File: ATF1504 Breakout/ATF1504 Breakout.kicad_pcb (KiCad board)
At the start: 2 copper layers, 73 x 52.5 mm, 12 parts, among them J1 Conn_01x20_Pin, J2 Conn_01x20_Pin, J3 Conn_01x02_Pin, P1 HDR-IDC-2.54-2X5P, U1 ATF1504ASV-xAx44, U2 TLV1117LV33DCYR

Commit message: route tracks and add graphics
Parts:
- added C3: 0.01u, easyeda2kicad:C0603, F.Cu at (175.8, 104.1)
- added R1: CLK ~{E}, easyeda2kicad:R0805, F.Cu at (176.0, 117.9)
- added REF**: KiCad-Logo_5mm_SilkScreen, Symbol:KiCad-Logo_5mm_SilkScreen, B.Cu at (180.9, 97.8)
- added REF**: OSHW-Logo2_9.8x8mm_SilkScreen, Symbol:OSHW-Logo2_9.8x8mm_SilkScreen, B.Cu at (180.1, 122.2)
- added U3: DSC1001CI4-002.0480T, easyeda2kicad:OSC-SMD_4P-L3.2-W2.5-BL_1C210000BB0F, F.Cu at (176.0, 110.3)
- C1, C2: value C_Polarized -> 1u; footprint easyeda2kicad:CAP-SMD_BD4.0-L4.3-W4.3-FD -> easyeda2kicad:C0603
- moved C2 16.3 mm to (190.3, 110.0)
- moved C1 11.5 mm to (185.5, 110.0), turned to 180 degrees
- moved U2 2.46 mm to (187.9, 101.0)
- moved H2 0.50 mm to (190.5, 129.5)
- moved H3 0.46 mm to (126.5, 129.5)
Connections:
- C1 pad 1: VCC -> +3.3V
- C2 pad 1: +3.3V -> VCC
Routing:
- net +3.3V: track 0.00 -> 201.9 mm
- net /JTAG_TCK: track 0.00 -> 53.3 mm, vias 0 -> 1
- net /JTAG_TDO: track 0.00 -> 42.9 mm, vias 0 -> 1
- net /JTAG_TDI: track 0.00 -> 42.6 mm
- net /JTAG_TMS: track 0.00 -> 36.9 mm, vias 0 -> 2
- net /PIN_22: track 0.00 -> 29.7 mm
- net /PIN_21: track 0.00 -> 28.3 mm
- net /PIN_23: track 0.00 -> 27.6 mm
- net /PIN_20: track 0.00 -> 26.9 mm
- net /PIN_25: track 0.00 -> 25.8 mm
- net /PIN_19: track 0.00 -> 25.5 mm
- net /PIN_2: track 0.00 -> 25.4 mm
- net /PIN_44: track 0.00 -> 24.7 mm
- net /PIN_18: track 0.00 -> 24.1 mm
- net /PIN_3: track 0.00 -> 24.1 mm
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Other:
- board text added: "ATF1504 Breakout v1"
- board text added: "GCLK1"
- board text added: "GCLR"
- board text added: "OE1"
- board text removed: "37"
- board text removed: "38"
- board text removed: "39"

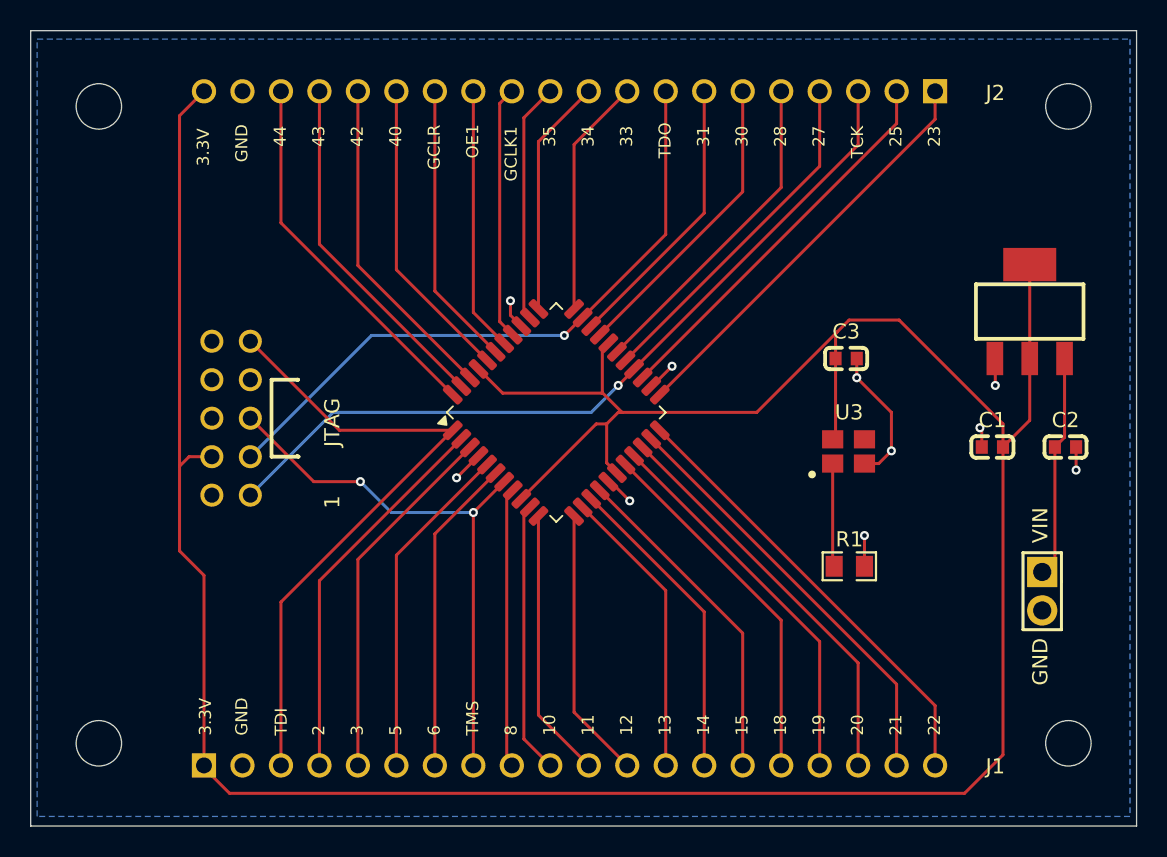
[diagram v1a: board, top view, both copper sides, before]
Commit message: add power-on-reset and switch and led peripherals
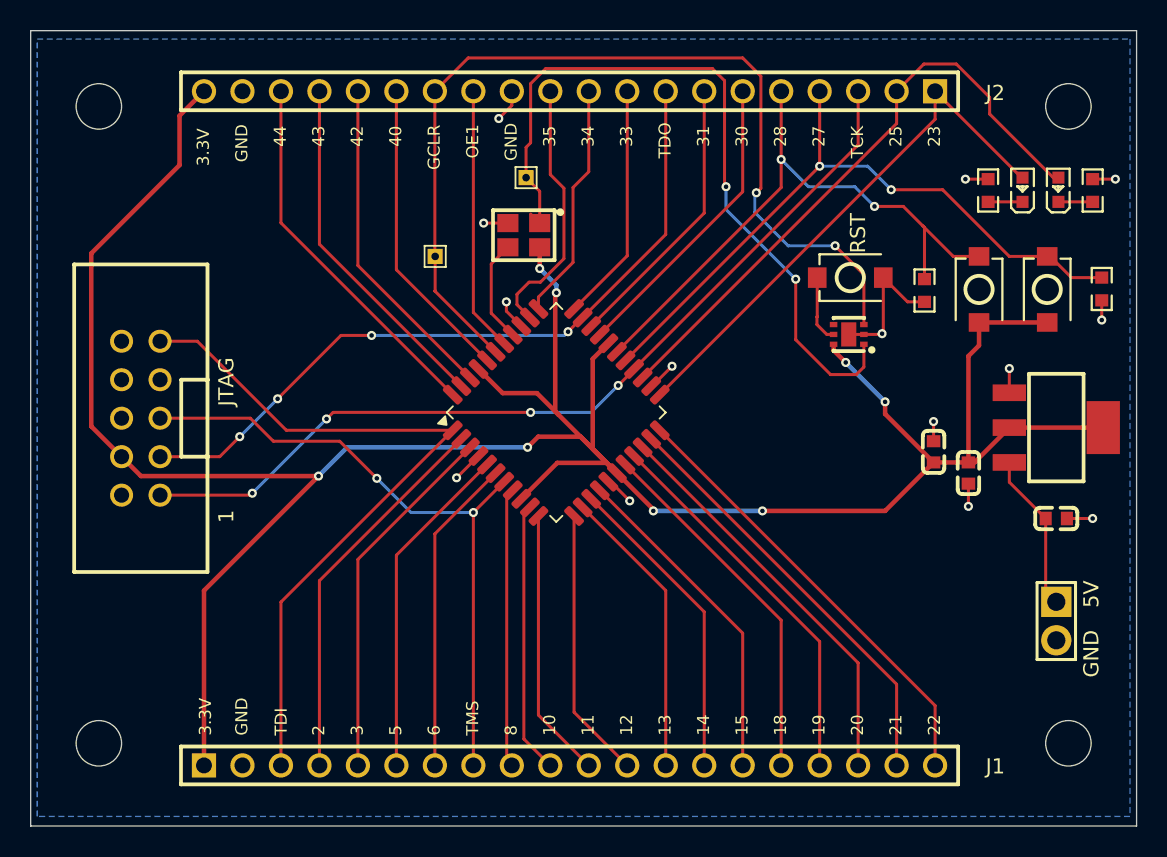
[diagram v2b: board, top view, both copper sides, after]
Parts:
- removed R1: CLK ~{E}, easyeda2kicad:R0805
- added D1: RED, easyeda2kicad:LED0603-RD_RED, F.Cu at (189.8, 93.0)
- added D2: YELLOW, easyeda2kicad:LED0603-RD-YELLOW, F.Cu at (187.5, 93.0)
- added R2: 50, easyeda2kicad:R0603, F.Cu at (192.1, 93.0)
- added R3: 50, easyeda2kicad:R0603, F.Cu at (185.2, 93.0)
- added R4: 10K, easyeda2kicad:R0603, F.Cu at (192.7, 99.5)
- added R5: 10K, easyeda2kicad:R0603, F.Cu at (181.0, 99.7)
- added SW1: TS-1088-AR02016, easyeda2kicad:SW-SMD_L3.9-W3.0-P4.45, F.Cu at (189.1, 99.6)
- added SW2: TS-1088-AR02016, easyeda2kicad:SW-SMD_L3.9-W3.0-P4.45, F.Cu at (184.6, 99.6)
- added SW3: TS-1088-AR02016, easyeda2kicad:SW-SMD_L3.9-W3.0-P4.45, F.Cu at (176.1, 98.8)
- added TP1: TestPoint, TestPoint:TestPoint_THTPad_1.0x1.0mm_Drill0.5mm, F.Cu at (148.7, 97.4)
- added TP2: TestPoint, TestPoint:TestPoint_THTPad_1.0x1.0mm_Drill0.5mm, F.Cu at (154.7, 92.2)
- added U4: MIC826YYMT-TR, easyeda2kicad:TDFN-6_L2.0-W2.0-P0.65-TL-EP, F.Cu at (176.0, 102.5)
- moved U3 25.8 mm to (154.6, 96.0), turned to 180 degrees
- moved C3 8.44 mm to (181.6, 110.3), turned to 90 degrees
- moved U2 7.86 mm to (189.7, 108.7), turned to 180 degrees
- moved P1 5.96 mm to (129.3, 108.1)
- moved C2 4.76 mm to (189.7, 114.7)
- moved C1 2.34 mm to (183.9, 111.7), turned to -90 degrees
- moved J3 2.18 mm to (189.7, 121.5)
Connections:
- net /PIN_39 renamed /GCLR
- J2 pad 12: /PIN_37 -> GND
- U1 pad 37: /PIN_37 -> /GCLK1
- U3 pad 1: Net-(U3-~{Standby}) -> /~{RST}
- U3 pad 3: /XCLK1 -> /GCLK1
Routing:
- net /~{RST}: track 0.00 -> 50.4 mm, vias 0 -> 2
- net /GCLR: track 18.9 -> 63.2 mm, vias 0 -> 2
- net /PIN_27: track 23.1 -> 44.7 mm, vias 0 -> 2
- net /PIN_28: track 21.7 -> 41.1 mm, vias 0 -> 2
- net /PIN_37: track 16.8 -> 0.00 mm
- net /PIN_25: track 25.8 -> 41.0 mm
- net +3.3V: track 201.9 -> 187.1 mm, vias 0 -> 8
- net GND: track 23.7 -> 32.0 mm, vias 10 -> 14
- net /PIN_23: track 27.6 -> 35.7 mm
- net Net-(U3-~{Standby}): track 6.82 -> 0.00 mm
- net /GCLK1: track 0.00 -> 6.81 mm
- net /JTAG_TCK: track 53.3 -> 59.4 mm, vias 1 -> 4
- net /JTAG_TDI: track 42.6 -> 48.6 mm
- net /JTAG_TMS: track 36.9 -> 42.8 mm
- net /JTAG_TDO: track 42.9 -> 48.9 mm, vias 1 -> 4
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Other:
- board text added: "5V"
- board text added: "RST"
- board text removed: "GCLK1"
- board text removed: "VIN"

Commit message: replace two of the mounting holes with tooling holes for assembly
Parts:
- H1, H3: footprint MountingHole:MountingHole_3mm -> MountingHole:ToolingHole_1.152mm
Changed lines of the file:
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@@
 		(embedded_fonts no)
 	)
-	(footprint "MountingHole:MountingHole_3mm"
+	(footprint "MountingHole:ToolingHole_1.152mm"
 		(layer "F.Cu")
 		(at 126.5 129.54)
-		(descr "Mounting Hole 3mm, no annular, generated by kicad-footprint-generator mountinghole.py")
-		(tags "mountinghole")
+		(descr "Tooling Hole 1.152mm, 1.3mm solder mask, JLCPCB specification, https://jlcpcb.com/help/article/How-to-add-tooling-holes-for-PCB-assembly-order")
+		(tags "mounting")
 		(property "Reference" "H3"
-			(at 0 -3.95 0)
+			(at 0 -1.5 0)
 			(layer "F.SilkS")
 			(hide yes)
@@
 		)
 		(property "Value" "MountingHole"
-			(at 0 3.95 0)
-			(layer "F.Fab")
-			(effects
-				(font
-					(size 1 1)
-					(thickness 0.15)
-				)
-			)
-		)
-		(property "Datasheet" "~"
+			(at 0 1.6 0)
+			(layer "F.Fab")
+			(effects
+				(font
+					(size 1 1)
+					(thickness 0.15)
+				)
+			)
+		)
+		(property "Datasheet" ""
 			(at 0 0 0)
+			(unlocked yes)
 			(layer "F.Fab")
 			(hide yes)
@@
 			)
 		)
-		(property "Description" "Mounting Hole without connection"
+		(property "Description" ""
 			(at 0 0 0)
+			(unlocked yes)
 			(layer "F.Fab")
 			(hide yes)
@@
 		(fp_circle
 			(center 0 0)
-			(end 3 0)
-			(stroke
-				(width 0.15)
-				(type solid)
-			)
-			(fill no)
-			(layer "Cmts.User")
-		)
-		(fp_circle
-			(center 0 0)
-			(end 3.25 0)
+			(end 0.7 0)
 			(stroke
 				(width 0.05)
@@
 		(pad "" np_thru_hole circle
 			(at 0 0)
-			(size 3 3)
-			(drill 3)
-			(layers "*.Cu" "*.Mask")
+			(size 1.152 1.152)
+			(drill 1.152)
+			(layers "*.Cu" "*.Mask")
+			(solder_mask_margin 0.074)
+		)
+		(zone
+			(net 0)
+			(net_name "")
+			(layers "F.Cu" "B.Cu")
+			(hatch edge 0.5)
+			(connect_pads
+				(clearance 0)
+			)
+			(min_thickness 0.25)
+			(filled_areas_thickness no)
+			(keepout
+				(tracks not_allowed)
+				(vias allowed)
+				(pads allowed)
+				(copperpour not_allowed)
+				(footprints not_allowed)
+			)
+			(placement
+				(enabled no)
+				(sheetname "")
+			)
+			(fill
+				(thermal_gap 0.5)
+				(thermal_bridge_width 0.5)
+			)
+			(polygon
+				(pts
+					(xy 127.2 129.54) (xy 127.179659 129.372479) (xy 127.119819 129.214694) (xy 127.023958 129.075814)
+					(xy 126.897645 128.963911) (xy 126.748223 128.885489) (xy 126.584376 128.845104) (xy 126.415624 128.845104)
+					(xy 126.251777 128.885489) (xy 126.102355 128.963911) (xy 125.976042 129.075814) (xy 125.880181 129.214694)
+					(xy 125.820341 129.372479) (xy 125.8 129.54) (xy 125.820341 129.707521) (xy 125.880181 129.865306)
+					(xy 125.976042 130.004186) (xy 126.102355 130.116089) (xy 126.251777 130.194511) (xy 126.415624 130.234896)
+					(xy 126.584376 130.234896) (xy 126.748223 130.194511) (xy 126.897645 130.116089) (xy 127.023958 130.004186)
+					(xy 127.119819 129.865306) (xy 127.179659 129.707521)
+				)
+			)
 		)
 		(embedded_fonts no)
@@
 		)
 	)
-	(footprint "MountingHole:MountingHole_3mm"
+	(footprint "MountingHole:ToolingHole_1.152mm"
 		(layer "F.Cu")
 		(at 190.5 87.5)
-		(descr "Mounting Hole 3mm, no annular, generated by kicad-footprint-generator mountinghole.py")
-		(tags "mountinghole")
+		(descr "Tooling Hole 1.152mm, 1.3mm solder mask, JLCPCB specification, https://jlcpcb.com/help/article/How-to-add-tooling-holes-for-PCB-assembly-order")
+		(tags "mounting")
 		(property "Reference" "H1"
-			(at 0 -3.95 0)
+			(at 0 -1.5 0)
 			(layer "F.SilkS")
 			(hide yes)
@@
 		)
 		(property "Value" "MountingHole"
-			(at 0 3.95 0)
-			(layer "F.Fab")
-			(effects
-				(font
-					(size 1 1)
-					(thickness 0.15)
-				)
-			)
-		)
-		(property "Datasheet" "~"
+			(at 0 1.6 0)
+			(layer "F.Fab")
+			(effects
+				(font
+					(size 1 1)
+					(thickness 0.15)
+				)
+			)
+		)
+		(property "Datasheet" ""
 			(at 0 0 0)
+			(unlocked yes)
 			(layer "F.Fab")
 			(hide yes)
@@
 			)
 		)
-		(property "Description" "Mounting Hole without connection"
+		(property "Description" ""
 			(at 0 0 0)
+			(unlocked yes)
 			(layer "F.Fab")
 			(hide yes)
@@
 		(fp_circle
 			(center 0 0)
-			(end 3 0)
-			(stroke
-				(width 0.15)
-				(type solid)
-			)
-			(fill no)
-			(layer "Cmts.User")
-		)
-		(fp_circle
-			(center 0 0)
-			(end 3.25 0)
+			(end 0.7 0)
 			(stroke
 				(width 0.05)
@@
 		(pad "" np_thru_hole circle
 			(at 0 0)
-			(size 3 3)
-			(drill 3)
-			(layers "*.Cu" "*.Mask")
+			(size 1.152 1.152)
+			(drill 1.152)
+			(layers "*.Cu" "*.Mask")
+			(solder_mask_margin 0.074)
+		)
+		(zone
+			(net 0)
+			(net_name "")
+			(layers "F.Cu" "B.Cu")
+			(hatch edge 0.5)
+			(connect_pads
+				(clearance 0)
+			)
+			(min_thickness 0.25)
+			(filled_areas_thickness no)
+			(keepout
+				(tracks not_allowed)
+				(vias allowed)
+				(pads allowed)
+				(copperpour not_allowed)
+				(footprints not_allowed)
+			)
+			(placement
+				(enabled no)
+				(sheetname "")
+			)
+			(fill
+				(thermal_gap 0.5)
+				(thermal_bridge_width 0.5)
+			)
+			(polygon
+				(pts
+					(xy 191.2 87.5) (xy 191.179659 87.332479) (xy 191.119819 87.174694) (xy 191.023958 87.035814) (xy 190.897645 86.923911)
+					(xy 190.748223 86.845489) (xy 190.584376 86.805104) (xy 190.415624 86.805104) (xy 190.251777 86.845489)
+					(xy 190.102355 86.923911) (xy 189.976042 87.035814) (xy 189.880181 87.174694) (xy 189.820341 87.332479)
+					(xy 189.8 87.5) (xy 189.820341 87.667521) (xy 189.880181 87.825306) (xy 189.976042 87.964186) (xy 190.102355 88.076089)
+					(xy 190.251777 88.154511) (xy 190.415624 88.194896) (xy 190.584376 88.194896) (xy 190.748223 88.154511)
+					(xy 190.897645 88.076089) (xy 191.023958 87.964186) (xy 191.119819 87.825306) (xy 191.179659 87.667521)
+				)
+			)
 		)
 		(embedded_fonts no)
